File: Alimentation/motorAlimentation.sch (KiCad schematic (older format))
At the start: 27 parts, among them P1 CONN_2, P2 CONN_2, Q1 2N2222, Q2 2N2222, Q3 2N2907, Q4 FDS4675, Q5 2N2222, U1 INA213, U2 LT1721

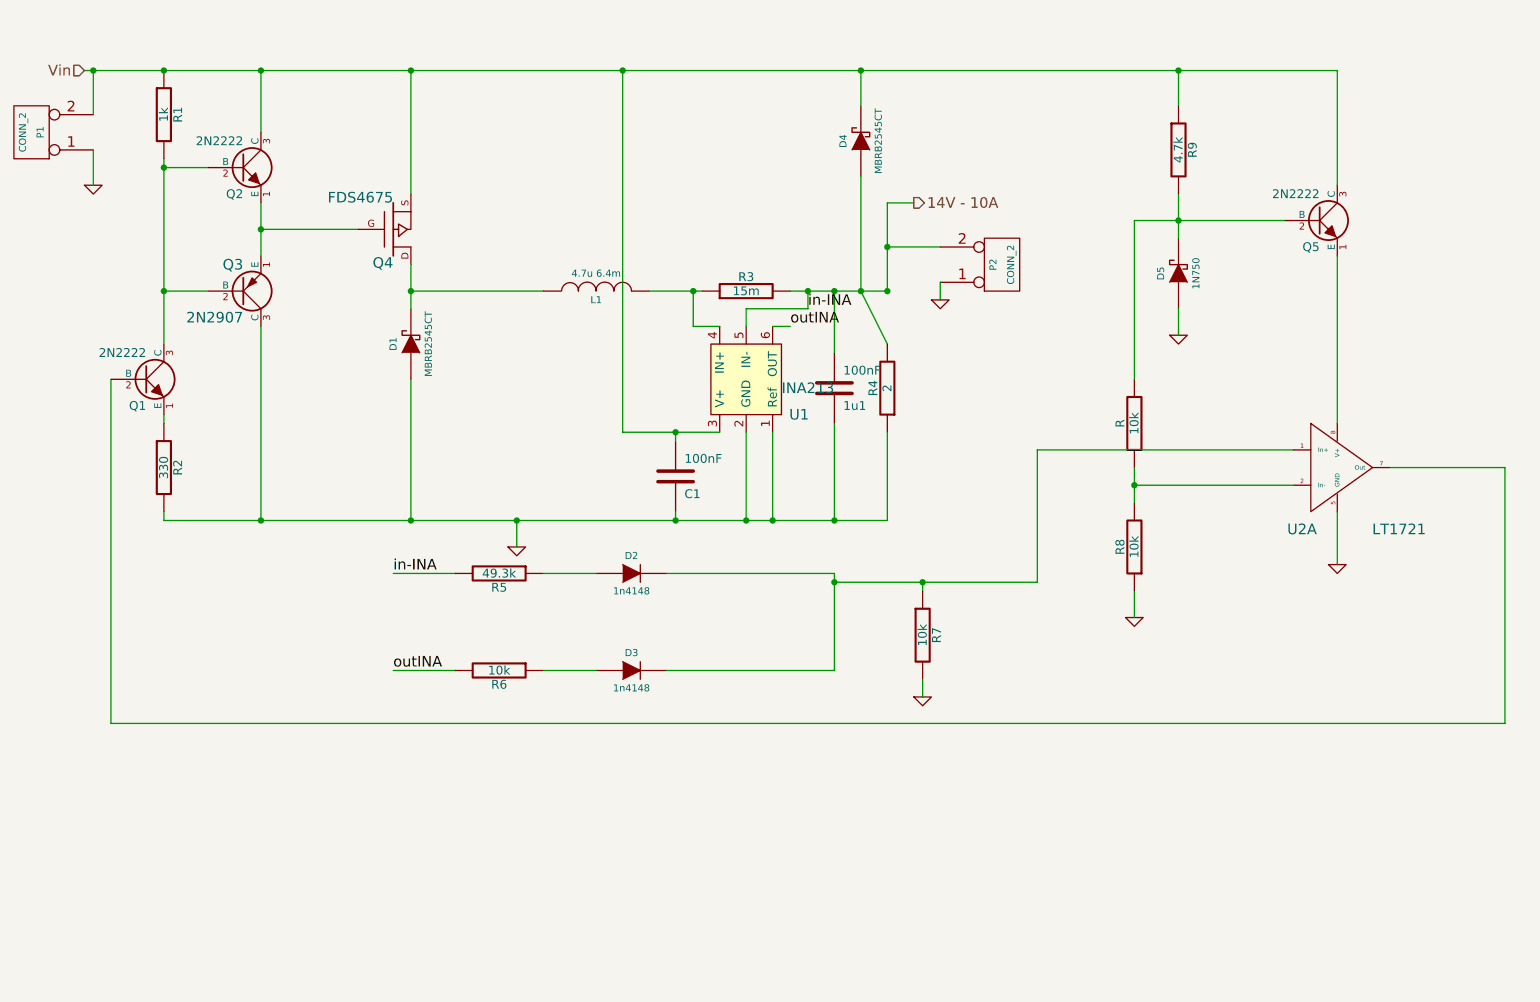
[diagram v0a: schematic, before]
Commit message: Adding board for alimentation
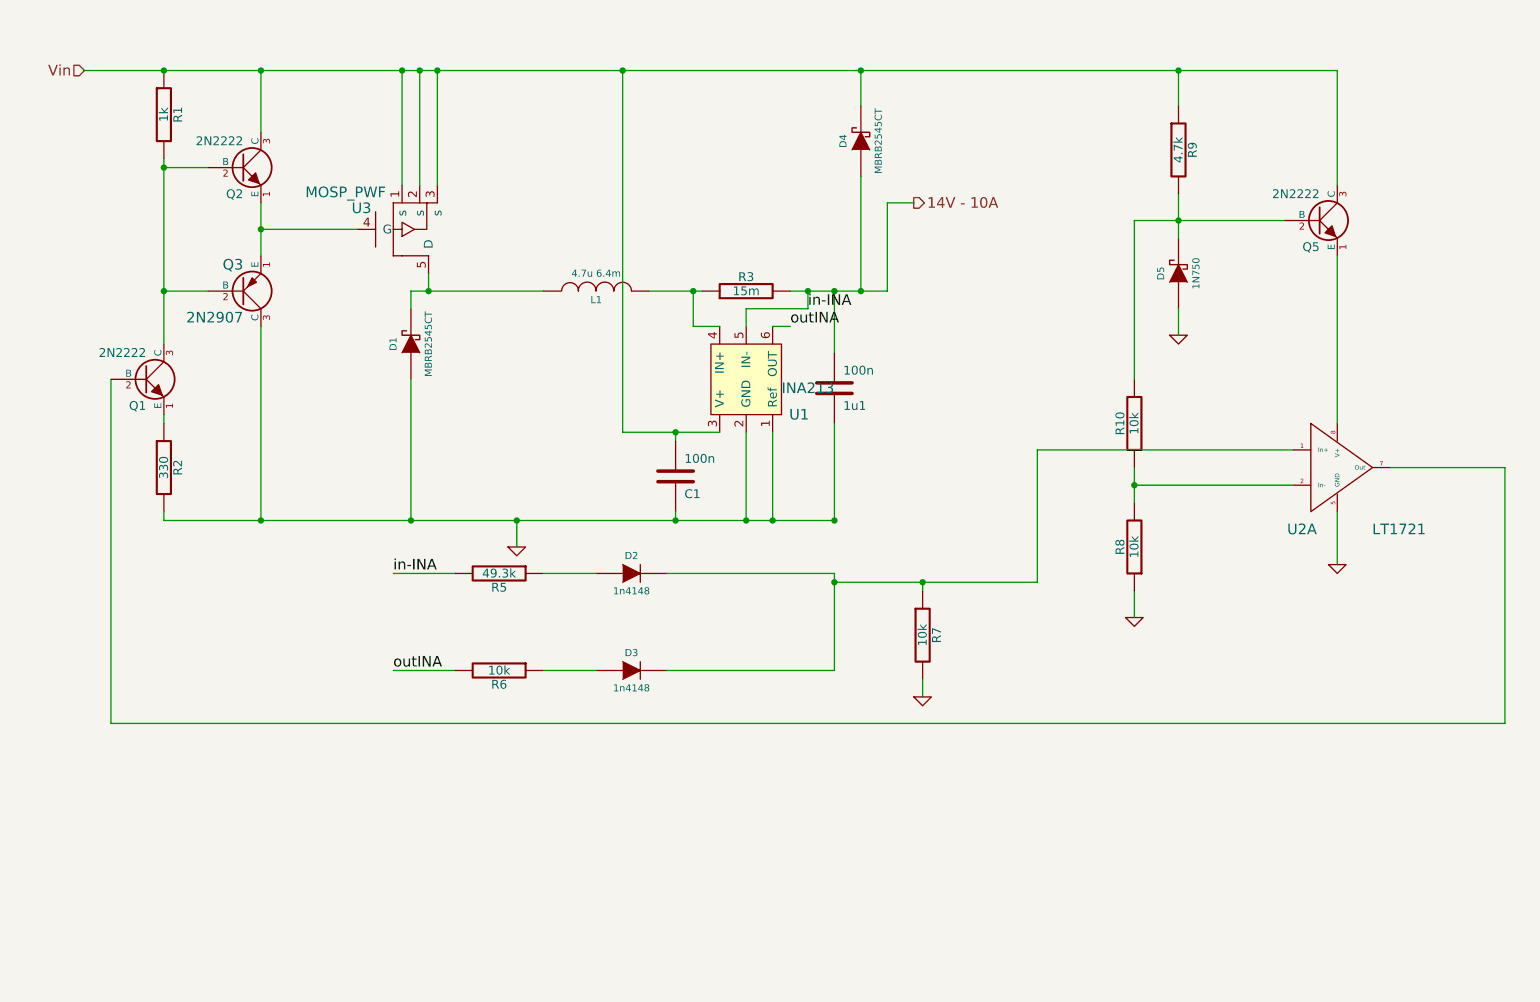
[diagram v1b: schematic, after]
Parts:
- removed P1, P2: CONN_2, symbol CONN_2
- removed Q4: FDS4675, symbol MOS_P
- removed R4: 2, symbol R
- added U3: MOSP_PWF, symbol MOSP_PWF
- 1u1, C1: value 100nF -> 100n
- renumbered R to R10
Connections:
- net Vin: now also U3.1 (s), U3.2 (s), U3.3 (s)
- net at D1.2 (K), L1.1: now also U3.5 (D)
- net at Q2.1 (E), Q3.1 (E): now also U3.4 (G)

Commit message: Debugging made on Alimentation, need thermal plan
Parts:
- removed Q1, Q2, Q5: 2N2222, symbol NPN
- removed Q3: 2N2907, symbol PNP
- added C9: 100n, symbol C
- added Q1, Q2, Q4: BCV27, symbol NPN_P
- added Q3: FMMT591, symbol PNP_P
- added R11: 470k, symbol R
- D1, D4: value MBRB2545CT -> STPS3045DJF
- D2, D3: value 1n4148 -> BAS16LT1G
- D5: value 1N750 -> BZX84
- U3: value MOSP_PWF -> SI7101DN-T1-GE3
- renumbered 1u1 to C8
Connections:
- wire segments 66 -> 74
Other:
- moved on the sheet: R10
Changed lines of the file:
@@
 $EndDescr
 Wire Wire Line
-	5800 2200 5800 2700
+	5800 2700 5800 2200
 Connection ~ 4600 4000
 Wire Wire Line
@@
 Connection ~ 3150 1450
 Wire Wire Line
-	3150 2100 3150 1450
+	3150 1450 3150 2100
 Connection ~ 3200 2700
 Wire Wire Line
 	3200 2600 3200 2700
-Wire Wire Line
-	8100 3600 6650 3600
-Wire Wire Line
-	8100 3800 7200 3800
 Wire Wire Line
 	3700 4000 3700 4150
@@
 Connection ~ 7450 1450
 Wire Wire Line
-	7450 1650 7450 1450
+	7450 1450 7450 1650
 Wire Wire Line
 	3350 4300 3000 4300
@@
 Wire Wire Line
 	8350 3950 8350 4250
-Connection ~ 7200 3800
-Wire Wire Line
-	7200 3200 7200 2300
+Wire Wire Line
+	7200 2900 7200 2300
 Wire Wire Line
 	7200 2300 8050 2300
@@
 	7450 2800 7450 2950
 Wire Wire Line
-	8350 2100 8350 1450
-Wire Wire Line
-	7450 2400 7450 2150
+	8350 1450 8350 2100
+Wire Wire Line
+	7450 2150 7450 2400
 Wire Wire Line
 	5350 2800 5000 2800
@@
 	1950 2000 1700 2000
 Wire Wire Line
-	2250 2500 2250 2200
+	2250 2200 2250 2500
 Wire Wire Line
 	5800 2200 5950 2200
 Wire Wire Line
-	3850 2700 3100 2700
+	3100 2700 3850 2700
 Wire Wire Line
 	3100 2700 3100 2800
@@
 Connection ~ 4600 3500
 Wire Wire Line
-	8350 1450 1250 1450
+	1250 1450 8350 1450
 Connection ~ 5650 1450
 Connection ~ 7450 2300
@@
 	8350 2500 8350 3450
 Wire Wire Line
-	7200 3700 7200 3900
+	7200 3400 7200 3900
 Wire Wire Line
 	7200 4400 7200 4550
@@
 	3350 4850 3000 4850
 Wire Wire Line
-	5800 2700 5250 2700
+	5250 2700 5800 2700
 Wire Wire Line
 	5500 4000 5500 3450
@@
 Wire Wire Line
 	9300 3700 9300 5150
-Wire Wire Line
-	6650 4350 6650 3600
 Wire Wire Line
 	3050 1450 3050 2100
@@
 P 2950 2350
 F 0 "U3" H 2820 2230 60  0000 C CNN
-F 1 "MOSP_PWF" H 2730 2140 60  0000 C CNN
+F 1 "SI7101DN-T1-GE3" H 2730 2140 60  0000 C CNN
 F 2 "" H 2950 2350 60  0001 C CNN
 F 3 "" H 2950 2350 60  0001 C CNN
@@
 $EndComp
 $Comp
-L GND #PWR08
+L GND #PWR9
 U 1 1 5320418A
 P 3700 4150
-F 0 "#PWR08" H 3700 4150 30  0001 C CNN
+F 0 "#PWR9" H 3700 4150 30  0001 C CNN
 F 1 "GND" H 3700 4080 30  0001 C CNN
 F 2 "" H 3700 4150 60  0001 C CNN
@@
 $EndComp
 $Comp
-L C 1u1
+L C C8
 U 1 1 53204173
 P 5500 3250
-F 0 "1u1" H 5550 3350 50  0000 L CNN
+F 0 "C8" H 5550 3350 50  0000 L CNN
 F 1 "100n" H 5550 3150 50  0000 L CNN
 F 2 "" H 5500 3250 60  0001 C CNN
@@
 P 4350 4300
 F 0 "D2" H 4350 4400 40  0000 C CNN
-F 1 "1n4148" H 4350 4200 40  0000 C CNN
+F 1 "BAS16LT1G" H 4350 4200 40  0000 C CNN
 F 2 "" H 4350 4300 60  0001 C CNN
 F 3 "" H 4350 4300 60  0001 C CNN
@@
 P 4350 4850
 F 0 "D3" H 4350 4950 40  0000 C CNN
-F 1 "1n4148" H 4350 4750 40  0000 C CNN
+F 1 "BAS16LT1G" H 4350 4750 40  0000 C CNN
 F 2 "" H 4350 4850 60  0001 C CNN
 F 3 "" H 4350 4850 60  0001 C CNN
@@
 $EndComp
 $Comp
-L GND #PWR09
+L GND #PWR10
 U 1 1 53204071
 P 6000 5000
-F 0 "#PWR09" H 6000 5000 30  0001 C CNN
+F 0 "#PWR10" H 6000 5000 30  0001 C CNN
 F 1 "GND" H 6000 4930 30  0001 C CNN
 F 2 "" H 6000 5000 60  0001 C CNN
@@
 $EndComp
 $Comp
-L GND #PWR010
+L GND #PWR13
 U 1 1 5320400C
 P 8350 4250
-F 0 "#PWR010" H 8350 4250 30  0001 C CNN
+F 0 "#PWR13" H 8350 4250 30  0001 C CNN
 F 1 "GND" H 8350 4180 30  0001 C CNN
 F 2 "" H 8350 4250 60  0001 C CNN
@@
 $EndComp
 $Comp
-L GND #PWR011
+L GND #PWR11
 U 1 1 53204000
 P 7200 4550
-F 0 "#PWR011" H 7200 4550 30  0001 C CNN
+F 0 "#PWR11" H 7200 4550 30  0001 C CNN
 F 1 "GND" H 7200 4480 30  0001 C CNN
 F 2 "" H 7200 4550 60  0001 C CNN
@@
 L R R10
 U 1 1 53203FB9
-P 7200 3450
-F 0 "R10" V 7280 3450 50  0000 C CNN
-F 1 "10k" V 7200 3450 50  0000 C CNN
-F 2 "" H 7200 3450 60  0001 C CNN
-F 3 "" H 7200 3450 60  0001 C CNN
-	1    7200 3450
+P 7200 3150
+F 0 "R10" V 7280 3150 50  0000 C CNN
+F 1 "10k" V 7200 3150 50  0000 C CNN
+F 2 "" H 7200 3150 60  0001 C CNN
+F 3 "" H 7200 3150 60  0001 C CNN
+	1    7200 3150
 	-1   0    0    1
 $EndComp
 $Comp
-L GND #PWR012
+L GND #PWR12
 U 1 1 53203FAE
 P 7450 2950
-F 0 "#PWR012" H 7450 2950 30  0001 C CNN
+F 0 "#PWR12" H 7450 2950 30  0001 C CNN
 F 1 "GND" H 7450 2880 30  0001 C CNN
 F 2 "" H 7450 2950 60  0001 C CNN
 F 3 "" H 7450 2950 60  0001 C CNN
 	1    7450 2950
-	1    0    0    -1
-$EndComp
-$Comp
-L NPN Q5
-U 1 1 532039D1
-P 8250 2300
-F 0 "Q5" H 8250 2150 50  0000 R CNN
-F 1 "2N2222" H 8250 2450 50  0000 R CNN
-F 2 "" H 8250 2300 60  0001 C CNN
-F 3 "" H 8250 2300 60  0001 C CNN
-	1    8250 2300
 	1    0    0    -1
 $EndComp
@@
 P 7450 2600
 F 0 "D5" H 7450 2700 40  0000 C CNN
-F 1 "1N750" H 7450 2500 40  0000 C CNN
+F 1 "BZX84" H 7450 2500 40  0000 C CNN
 F 2 "" H 7450 2600 60  0001 C CNN
 F 3 "" H 7450 2600 60  0001 C CNN
@@
 P 5650 1850
 F 0 "D4" H 5650 1950 40  0000 C CNN
-F 1 "MBRB2545CT" H 5650 1750 40  0000 C CNN
+F 1 "STPS3045DJF" H 5650 1750 40  0000 C CNN
 F 2 "" H 5650 1850 60  0001 C CNN
 F 3 "" H 5650 1850 60  0001 C CNN
@@
 $EndComp
 $Comp
-L NPN Q1
-U 1 1 532035E6
-P 1600 3200
-F 0 "Q1" H 1600 3050 50  0000 R CNN
-F 1 "2N2222" H 1600 3350 50  0000 R CNN
-F 2 "" H 1600 3200 60  0001 C CNN
-F 3 "" H 1600 3200 60  0001 C CNN
-	1    1600 3200
-	1    0    0    -1
-$EndComp
-$Comp
-L NPN Q2
-U 1 1 532035D5
-P 2150 2000
-F 0 "Q2" H 2150 1850 50  0000 R CNN
-F 1 "2N2222" H 2150 2150 50  0000 R CNN
-F 2 "" H 2150 2000 60  0001 C CNN
-F 3 "" H 2150 2000 60  0001 C CNN
-	1    2150 2000
-	1    0    0    -1
-$EndComp
-$Comp
-L PNP Q3
-U 1 1 532035CD
-P 2150 2700
-F 0 "Q3" H 2150 2550 60  0000 R CNN
-F 1 "2N2907" H 2150 2850 60  0000 R CNN
-F 2 "" H 2150 2700 60  0001 C CNN
-F 3 "" H 2150 2700 60  0001 C CNN
-	1    2150 2700
-	1    0    0    1
-$EndComp
-$Comp
 L DIODESCH D1
 U 1 1 5320353D
 P 3100 3000
 F 0 "D1" H 3100 3100 40  0000 C CNN
-F 1 "MBRB2545CT" H 3100 2900 40  0000 C CNN
+F 1 "STPS3045DJF" H 3100 2900 40  0000 C CNN
 F 2 "" H 3100 3000 60  0001 C CNN
 F 3 "" H 3100 3000 60  0001 C CNN
@@
 Text HLabel 5950 2200 2    60   Output ~ 0
 14V - 10A
+Wire Wire Line
+	7200 3600 8100 3600
+Connection ~ 7200 3600
+Wire Wire Line
+	8100 3800 6650 3800
+Wire Wire Line
+	6650 3800 6650 4350
+$Comp
+L NPN_P Q1
+U 1 1 5363B8C6
+P 1600 3200
+F 0 "Q1" H 1600 3050 50  0000 R CNN
+F 1 "BCV27" H 1600 3350 50  0000 R CNN
+F 2 "" H 1600 3200 60  0000 C CNN
+F 3 "" H 1600 3200 60  0000 C CNN
+	1    1600 3200
+	1    0    0    -1
+$EndComp
+$Comp
+L NPN_P Q2
+U 1 1 5363B8D3
+P 2150 2000
+F 0 "Q2" H 2150 1850 50  0000 R CNN
+F 1 "BCV27" H 2150 2150 50  0000 R CNN
+F 2 "" H 2150 2000 60  0000 C CNN
+F 3 "" H 2150 2000 60  0000 C CNN
+	1    2150 2000
+	1    0    0    -1
+$EndComp
+$Comp
+L NPN_P Q4
+U 1 1 5363B8DF
+P 8250 2300
+F 0 "Q4" H 8250 2150 50  0000 R CNN
+F 1 "BCV27" H 8250 2450 50  0000 R CNN
+F 2 "" H 8250 2300 60  0000 C CNN
+F 3 "" H 8250 2300 60  0000 C CNN
+	1    8250 2300
+	1    0    0    -1
+$EndComp
+$Comp
+L PNP_P Q3
+U 1 1 5363B8E7
+P 2150 2700
+F 0 "Q3" H 2150 2550 60  0000 R CNN
+F 1 "FMMT591" H 2150 2850 60  0000 R CNN
+F 2 "" H 2150 2700 60  0000 C CNN
+F 3 "" H 2150 2700 60  0000 C CNN
+	1    2150 2700
+	1    0    0    1
+$EndComp
+$Comp
+L R R11
+U 1 1 5379D32E
+P 8350 3150
+F 0 "R11" V 8430 3150 50  0000 C CNN
+F 1 "470k" V 8350 3150 50  0000 C CNN
+F 2 "" H 8350 3150 60  0001 C CNN
+F 3 "" H 8350 3150 60  0001 C CNN
+	1    8350 3150
+	0    1    1    0
+$EndComp
+Wire Wire Line
+	8100 3150 7750 3150
+Wire Wire Line
+	7750 3150 7750 3600
+Connection ~ 7750 3600
+Wire Wire Line
+	8600 3150 8950 3150
+Wire Wire Line
+	8950 3150 8950 3700
+Connection ~ 8950 3700
+$Comp
+L C C9
+U 1 1 5379D435
+P 8750 4100
+F 0 "C9" H 8800 4200 50  0000 L CNN
+F 1 "100n" H 8800 4000 50  0000 L CNN
+F 2 "" H 8750 4100 60  0001 C CNN
+F 3 "" H 8750 4100 60  0001 C CNN
+	1    8750 4100
+	1    0    0    1
+$EndComp
+Wire Wire Line
+	8750 3900 8700 3350
+Wire Wire Line
+	8700 3350 8350 3350
+Connection ~ 8350 3350
+Wire Wire Line
+	8750 4300 8700 4100
+Wire Wire Line
+	8700 4100 8350 4100
+Connection ~ 8350 4100
 $EndSCHEMATC

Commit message: Adding alimentation security,starting new design
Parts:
- removed D1: STPS3045DJF, symbol DIODESCH
- added C15: 470p, symbol C
- added C16: 100n, symbol C
- added D1: Z-10V, symbol ZENERSMALL
- added Q5: 2N7002, symbol MOS_N2
- added R12, R14, R15: 1k, symbol R
- added R13: 3k, symbol R
- added R16: 10k, symbol R
- added U5, U6: BAS16LT1G, symbol DIODE-SOT23
- added U7: 74HC1G14, symbol 74HC1G14
- added U8: MOSN_PWF, symbol MOSN_PWF
- C8: value 100n -> 20u
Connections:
- net labels added: cmdNmos
- wire segments 74 -> 108

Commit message: Add 5V LDO for logic part of motor alimentation
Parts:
- removed D5: BZX84, symbol DIODESCH
- removed Q4: BCV27, symbol NPN_P
- removed R9: 4.7k, symbol R
- added C17: 330n, symbol C
- added C18: 100n, symbol C
- added U9: L78L05, symbol L78L05
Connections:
- net labels added: +5V
- wire segments 108 -> 111
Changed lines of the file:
@@
 Wire Wire Line
 	5500 2700 5500 3050
-Connection ~ 7450 1450
-Wire Wire Line
-	7450 1450 7450 1650
 Wire Wire Line
 	3350 4300 3000 4300
@@
 Wire Wire Line
 	7200 2900 7200 2300
-Wire Wire Line
-	7200 2300 8050 2300
-Wire Wire Line
-	7450 2800 7450 2950
-Wire Wire Line
-	8350 1450 8350 2100
-Wire Wire Line
-	7450 2150 7450 2400
 Wire Wire Line
 	5350 2800 5000 2800
@@
 	1250 1450 8350 1450
 Connection ~ 5650 1450
-Connection ~ 7450 2300
 Wire Wire Line
 	8350 2500 8350 3450
@@
 $EndComp
 $Comp
-L GND #PWR09
+L GND #PWR14
 U 1 1 5320418A
 P 3700 4150
-F 0 "#PWR09" H 3700 4150 30  0001 C CNN
+F 0 "#PWR14" H 3700 4150 30  0001 C CNN
 F 1 "GND" H 3700 4080 30  0001 C CNN
 F 2 "" H 3700 4150 60  0001 C CNN
@@
 $EndComp
 $Comp
-L GND #PWR010
+L GND #PWR16
 U 1 1 53204071
 P 6000 5000
-F 0 "#PWR010" H 6000 5000 30  0001 C CNN
+F 0 "#PWR16" H 6000 5000 30  0001 C CNN
 F 1 "GND" H 6000 4930 30  0001 C CNN
 F 2 "" H 6000 5000 60  0001 C CNN
@@
 $EndComp
 $Comp
-L GND #PWR011
+L GND #PWR20
 U 1 1 5320400C
 P 8350 4250
-F 0 "#PWR011" H 8350 4250 30  0001 C CNN
+F 0 "#PWR20" H 8350 4250 30  0001 C CNN
 F 1 "GND" H 8350 4180 30  0001 C CNN
 F 2 "" H 8350 4250 60  0001 C CNN
@@
 $EndComp
 $Comp
-L GND #PWR012
+L GND #PWR18
 U 1 1 53204000
 P 7200 4550
-F 0 "#PWR012" H 7200 4550 30  0001 C CNN
+F 0 "#PWR18" H 7200 4550 30  0001 C CNN
 F 1 "GND" H 7200 4480 30  0001 C CNN
 F 2 "" H 7200 4550 60  0001 C CNN
@@
 	-1   0    0    1
 $EndComp
-$Comp
-L GND #PWR013
-U 1 1 53203FAE
-P 7450 2950
-F 0 "#PWR013" H 7450 2950 30  0001 C CNN
-F 1 "GND" H 7450 2880 30  0001 C CNN
-F 2 "" H 7450 2950 60  0001 C CNN
-F 3 "" H 7450 2950 60  0001 C CNN
-	1    7450 2950
-	1    0    0    -1
-$EndComp
 Text Label 5350 2800 0    60   ~ 0
 in-INA
@@
 outINA
 $Comp
-L DIODESCH D5
-U 1 1 532039F5
-P 7450 2600
-F 0 "D5" H 7450 2700 40  0000 C CNN
-F 1 "BZX84" H 7450 2500 40  0000 C CNN
-F 2 "" H 7450 2600 60  0001 C CNN
-F 3 "" H 7450 2600 60  0001 C CNN
-	1    7450 2600
-	0    -1   -1   0
-$EndComp
-$Comp
-L R R9
-U 1 1 532039E3
-P 7450 1900
-F 0 "R9" V 7530 1900 50  0000 C CNN
-F 1 "4.7k" V 7450 1900 50  0000 C CNN
-F 2 "" H 7450 1900 60  0001 C CNN
-F 3 "" H 7450 1900 60  0001 C CNN
-	1    7450 1900
-	1    0    0    -1
-$EndComp
-$Comp
 L DIODESCH D4
 U 1 1 5320363F
@@
 $EndComp
 $Comp
-L NPN_P Q4
-U 1 1 5363B8DF
-P 8250 2300
-F 0 "Q4" H 8250 2150 50  0000 R CNN
-F 1 "BCV27" H 8250 2450 50  0000 R CNN
-F 2 "" H 8250 2300 60  0000 C CNN
-F 3 "" H 8250 2300 60  0000 C CNN
-	1    8250 2300
-	1    0    0    -1
-$EndComp
-$Comp
 L PNP_P Q3
 U 1 1 5363B8E7
@@
 	1700 4400 1700 4500
 $Comp
-L GND #PWR014
+L GND #PWR9
 U 1 1 537DEE77
 P 1700 4500
-F 0 "#PWR014" H 1700 4500 30  0001 C CNN
+F 0 "#PWR9" H 1700 4500 30  0001 C CNN
 F 1 "GND" H 1700 4430 30  0001 C CNN
 F 2 "" H 1700 4500 60  0000 C CNN
@@
 $EndComp
 $Comp
-L GND #PWR015
+L GND #PWR12
 U 1 1 537DEEFD
 P 2100 4800
-F 0 "#PWR015" H 2100 4800 30  0001 C CNN
+F 0 "#PWR12" H 2100 4800 30  0001 C CNN
 F 1 "GND" H 2100 4730 30  0001 C CNN
 F 2 "" H 2100 4800 60  0000 C CNN
@@
 	2000 6000 2000 6200
 $Comp
-L GND #PWR016
+L GND #PWR11
 U 1 1 537E0495
 P 2000 6200
-F 0 "#PWR016" H 2000 6200 30  0001 C CNN
+F 0 "#PWR11" H 2000 6200 30  0001 C CNN
 F 1 "GND" H 2000 6130 30  0001 C CNN
 F 2 "" H 2000 6200 60  0000 C CNN
@@
 	1850 6350 1850 6400
 $Comp
-L GND #PWR017
+L GND #PWR10
 U 1 1 537E08EA
 P 1850 6400
-F 0 "#PWR017" H 1850 6400 30  0001 C CNN
+F 0 "#PWR10" H 1850 6400 30  0001 C CNN
 F 1 "GND" H 1850 6330 30  0001 C CNN
 F 2 "" H 1850 6400 60  0000 C CNN
@@
 	1150 5850 1150 4950
 Wire Wire Line
-	1400 4950 1150 4950
+	1150 4950 1400 4950
 Connection ~ 1400 4950
 $Comp
@@
 $EndComp
 $Comp
-L GND #PWR018
+L GND #PWR13
 U 1 1 537E0DD6
 P 2800 6600
-F 0 "#PWR018" H 2800 6600 30  0001 C CNN
+F 0 "#PWR13" H 2800 6600 30  0001 C CNN
 F 1 "GND" H 2800 6530 30  0001 C CNN
 F 2 "" H 2800 6600 60  0000 C CNN
@@
 Connection ~ 3750 5700
 $Comp
-L GND #PWR019
+L GND #PWR15
 U 1 1 537E1363
 P 3750 6300
-F 0 "#PWR019" H 3750 6300 30  0001 C CNN
+F 0 "#PWR15" H 3750 6300 30  0001 C CNN
 F 1 "GND" H 3750 6230 30  0001 C CNN
 F 2 "" H 3750 6300 60  0000 C CNN
@@
 Wire Wire Line
 	3750 6200 3750 6300
+$Comp
+L +5V #PWR17
+U 1 1 53AADE6C
+P 7200 2300
+F 0 "#PWR17" H 7200 2390 20  0001 C CNN
+F 1 "+5V" H 7200 2390 30  0000 C CNN
+F 2 "" H 7200 2300 60  0000 C CNN
+F 3 "" H 7200 2300 60  0000 C CNN
+	1    7200 2300
+	1    0    0    -1
+$EndComp
+$Comp
+L +5V #PWR19
+U 1 1 53AADE7B
+P 8350 2500
+F 0 "#PWR19" H 8350 2590 20  0001 C CNN
+F 1 "+5V" H 8350 2590 30  0000 C CNN
+F 2 "" H 8350 2500 60  0000 C CNN
+F 3 "" H 8350 2500 60  0000 C CNN
+	1    8350 2500
+	1    0    0    -1
+$EndComp
+$Comp
+L L78L05 U9
+U 1 1 53AAE227
+P 8650 1500
+F 0 "U9" H 8950 1350 60  0000 C CNN
+F 1 "L78L05" H 9050 1250 60  0000 C CNN
+F 2 "" H 8650 1500 60  0000 C CNN
+F 3 "" H 8650 1500 60  0000 C CNN
+	1    8650 1500
+	1    0    0    -1
+$EndComp
+Wire Wire Line
+	8950 1450 9250 1450
+Wire Wire Line
+	9250 1450 9250 1250
+$Comp
+L +5V #PWR22
+U 1 1 53AAE2CB
+P 9250 1250
+F 0 "#PWR22" H 9250 1340 20  0001 C CNN
+F 1 "+5V" H 9250 1340 30  0000 C CNN
+F 2 "" H 9250 1250 60  0000 C CNN
+F 3 "" H 9250 1250 60  0000 C CNN
+	1    9250 1250
+	1    0    0    -1
+$EndComp
+$Comp
+L GND #PWR21
+U 1 1 53AAE2DA
+P 8650 2100
+F 0 "#PWR21" H 8650 2100 30  0001 C CNN
+F 1 "GND" H 8650 2030 30  0001 C CNN
+F 2 "" H 8650 2100 60  0000 C CNN
+F 3 "" H 8650 2100 60  0000 C CNN
+	1    8650 2100
+	1    0    0    -1
+$EndComp
+Wire Wire Line
+	8650 1800 8650 2100
+$Comp
+L C C17
+U 1 1 53AAE37E
+P 8250 1750
+F 0 "C17" H 8300 1850 50  0000 L CNN
+F 1 "330n" H 8300 1650 50  0000 L CNN
+F 2 "" H 8250 1750 60  0000 C CNN
+F 3 "" H 8250 1750 60  0000 C CNN
+	1    8250 1750
+	1    0    0    -1
+$EndComp
+$Comp
+L C C18
+U 1 1 53AAE38D
+P 9150 1750
+F 0 "C18" H 9200 1850 50  0000 L CNN
+F 1 "100n" H 9200 1650 50  0000 L CNN
+F 2 "" H 9150 1750 60  0000 C CNN
+F 3 "" H 9150 1750 60  0000 C CNN
+	1    9150 1750
+	1    0    0    -1
+$EndComp
+Wire Wire Line
+	9150 1550 9150 1450
+Connection ~ 9150 1450
+Wire Wire Line
+	8250 1550 8250 1450
+Connection ~ 8250 1450
+Wire Wire Line
+	8250 1950 8250 2000
+Wire Wire Line
+	8250 2000 9150 2000
+Connection ~ 8650 2000
+Wire Wire Line
+	9150 2000 9150 1950
 $EndSCHEMATC
